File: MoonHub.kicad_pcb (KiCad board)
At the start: 4 copper layers, 250 x 16.5 mm, 33 parts, among them J1 USB_A, J2 USB_C_Receptacle_USB2.0, J3 USB_C_Receptacle_USB2.0, J4 USB_A, U1 SRV05-4, U2 SRV05-4, U3 CH334U, U4 TPS2552DBVR, Y1 12MHz

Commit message: second commmit
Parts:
- moved H4 83.8 mm to (164.2, 14.5)
- moved J2 65.1 mm to (157.1, 8.30)
- moved J4 47.9 mm to (190.9, 7.11)
- moved C8 4.90 mm to (204.3, 21.1)
- moved U1 1.50 mm to (27.8, 12.0)
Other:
- board size 250 x 16.5 mm -> 166.1 x 16.5 mm
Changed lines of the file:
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@@
   )
   (footprint "Capacitor_SMD:C_1206_3216Metric" (layer "F.Cu")
-    (at 200.775 24.5)
+    (at 204.3 21.1)
     (descr "Capacitor SMD 1206 (3216 Metric), square (rectangular) end terminal, IPC_7351 nominal, (Body size source: IPC-SM-782 page 76, https://www.pcb-3d.com/wordpress/wp-content/uploads/ipc-sm-782a_amendment_1_and_2.pdf), generated with kicad-footprint-generator")
     (tags "capacitor")
@@
         (effects (font (size 1 1) (thickness 0.15)))
     )
-    (pad "1" thru_hole circle (at 0 0) (size 3.500001 3.500001) (drill 2.2) (layers "*.Cu" "*.Mask")
+    (pad "1" thru_hole circle (at -83.7605 -0.1) (size 3.500001 3.500001) (drill 2.2) (layers "*.Cu" "*.Mask")
       (net 38 "GNDPWR") (pinfunction "1") (pintype "input"))
   )
@@
   )
   (footprint "MoonHub:Generic-Mounthole" (layer "F.Cu")
-    (at 248 14.5)
+    (at 164.2 14.5)
     (property "Sheetfile" "MoonHub.kicad_sch")
     (property "Sheetname" "")
@@
   )
   (footprint "MoonHub:TYPE-C-31-M-12" (layer "F.Cu")
-    (at 222.25 8.3 180)
+    (at 157.1375 8.3 180)
     (property "Sheetfile" "MoonHub.kicad_sch")
     (property "Sheetname" "")
@@
   )
   (footprint "MoonHub:USB-A-SMD_AF-APPLE-10.6" (layer "F.Cu")
-    (at 238.8 7.113 180)
+    (at 190.903 7.113 180)
     (property "Sheetfile" "MoonHub.kicad_sch")
     (property "Sheetname" "")
@@
   )
   (footprint "PCM_marbastlib-various:SOT-23-6-routable" (layer "F.Cu")
-    (at 27.75 10.5)
+    (at 27.75 12)
     (descr "SOT, 6 Pin (https://www.jedec.org/sites/default/files/docs/Mo-178c.PDF variant AB), generated with kicad-footprint-generator ipc_gullwing_generator.py")
     (tags "SOT TO_SOT_SMD")
@@
   (gr_line (start 0 14.5) (end 0 2)
     (stroke (width 0.1) (type default)) (layer "Edge.Cuts"))
-  (gr_line (start 250 14.5) (end 250 2)
+  (gr_line (start 166.1395 14.5) (end 166.1395 2)
     (stroke (width 0.1) (type default)) (layer "Edge.Cuts"))
-  (gr_arc (start 250 14.5) (mid 249.414214 15.914214) (end 248 16.5)
+  (gr_arc (start 166.1395 14.5) (mid 165.553714 15.914214) (end 164.1395 16.5)
     (stroke (width 0.1) (type default)) (layer "Edge.Cuts"))
   (gr_arc (start 2 16.5) (mid 0.585786 15.914214) (end 0 14.5)
@@
   (gr_arc (start 0 2) (mid 0.585786 0.585786) (end 2 0)
     (stroke (width 0.1) (type default)) (layer "Edge.Cuts"))
-  (gr_arc (start 248 0) (mid 249.414214 0.585786) (end 250 2)
+  (gr_arc (start 164.1395 0) (mid 165.553714 0.585786) (end 166.1395 2)
     (stroke (width 0.1) (type default)) (layer "Edge.Cuts"))
-  (gr_line (start 2 0) (end 248 0)
+  (gr_line (start 2 0) (end 164.1395 0)
     (stroke (width 0.1) (type default)) (layer "Edge.Cuts"))
-  (gr_line (start 248 16.5) (end 2 16.5)
+  (gr_line (start 164.1395 16.5) (end 2 16.5)
     (stroke (width 0.1) (type default)) (layer "Edge.Cuts"))
-  (segment (start 246.937 3.063) (end 247.9 2.1) (width 0.5) (layer "B.Cu") (net 38))
-  (segment (start 245.2 3.063) (end 246.937 3.063) (width 0.5) (layer "B.Cu") (net 38))
+  (segment (start 163.5395 2.6) (end 164.1395 2) (width 1) (layer "B.Cu") (net 38))
+  (segment (start 161.4375 2.6) (end 163.5395 2.6) (width 1) (layer "B.Cu") (net 38))
   (zone (net 6) (net_name "VBUS") (layer "F.Cu") (hatch edge 0.5)
     (priority 1)

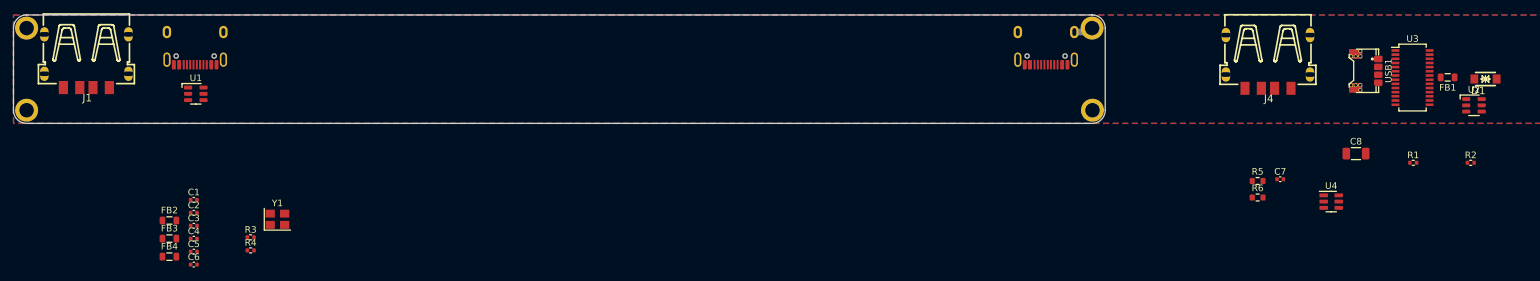
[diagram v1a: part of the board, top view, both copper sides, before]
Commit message: fully routed
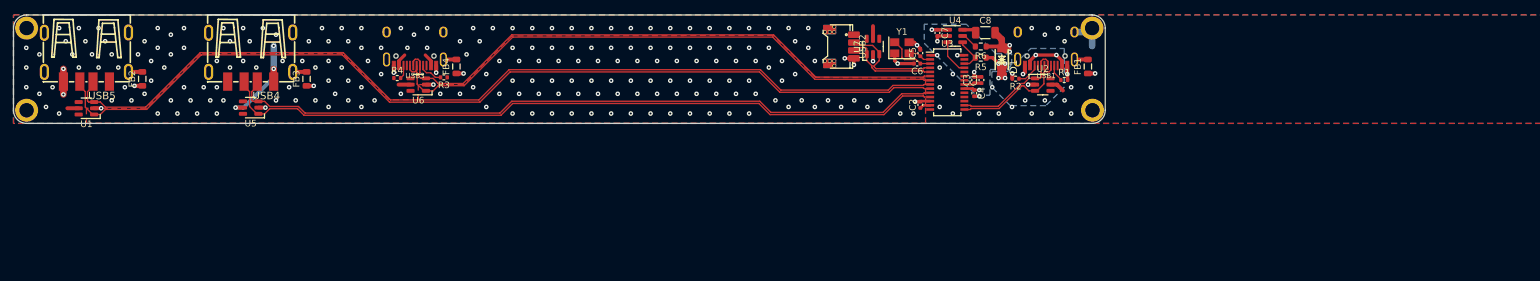
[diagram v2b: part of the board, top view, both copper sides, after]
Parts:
- added U5: SRV05-4, PCM_marbastlib-various:SOT-23-6-routable, F.Cu at (36.1, 14.1)
- added U6: SRV05-4, PCM_marbastlib-various:SOT-23-6-routable, F.Cu at (61.6, 10.6)
- added U7: SRV05-4, PCM_marbastlib-various:SOT-23-6-routable, F.Cu at (130.8, 4.80)
- USB1: renamed from J2; footprint MoonHub:TYPE-C-31-M-12 -> MoonHub:HRO-TYPE-C-31-M-12-Assembly
- USB2: renamed from USB1; footprint MoonHub:PicoEZMate-Reinforced-Alt -> MoonHub:PicoEZMate-Reinforced-Lite
- USB3: renamed from J3; footprint MoonHub:TYPE-C-31-M-12 -> MoonHub:HRO-TYPE-C-31-M-12-Assembly
- USB4: renamed from J4; footprint MoonHub:USB-A-SMD_AF-APPLE-10.6 -> MoonHub:USB-A-SMD_USB-M-21_914-441A2021S10200
- USB5: renamed from J1; footprint MoonHub:USB-A-SMD_AF-APPLE-10.6 -> MoonHub:USB-A-SMD_USB-M-21_914-441A2021S10200
- moved USB4 154.8 mm to (36.1, 6.40)
- moved C1 121.2 mm to (147.3, 9.90), turned to 90 degrees
- moved C3 120.8 mm to (146.2, 9.90), turned to 90 degrees
- moved C4 120.8 mm to (146.2, 11.9), turned to -90 degrees
- moved C5 114.6 mm to (138.0, 5.80), turned to 90 degrees
- moved C6 114.3 mm to (137.5, 7.40), turned to 180 degrees
- moved C2 111.8 mm to (138.0, 13.7), turned to 90 degrees
- moved Y1 98.5 mm to (135.2, 5.00)
- moved USB2 80.1 mm to (125.7, 4.80)
- moved D1 73.7 mm to (150.4, 6.80), turned to -90 degrees
- moved U3 70.8 mm to (142.1, 10.3)
- moved R2 70.4 mm to (152.5, 9.70), turned to 180 degrees
- moved U2 65.7 mm to (156.6, 10.6)
- moved U4 62.5 mm to (143.3, 3.20)
- moved C8 59.3 mm to (147.9, 2.70)
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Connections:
- C1 pad 1: +3V3 -> Net-(C1-Pad1)
- C2 pad 1: +3V3 -> Net-(C2-Pad1)
- C3 pad 1: +3V3 -> Net-(C1-Pad1)
- C5 pad 1: Net-(C5-Pad1) -> Net-(U3-XO)
- C6 pad 1: Net-(C6-Pad1) -> Net-(U3-XI)
- U1 pad 3: /USB2_D+ -> /USB1_D-
- U1 pad 4: /USB2_D- -> unconnected-(U1-IO3-Pad4)
- U1 pad 6: /USB1_D- -> unconnected-(U1-IO4-Pad6)
- U2 pad 3: /USB3_D+ -> /USBU_D-
- U2 pad 4: /USB3_D- -> unconnected-(U2-IO3-Pad4)
- U2 pad 6: /USBU_D- -> unconnected-(U2-IO4-Pad6)
- U3 pad 10: /USB1_D- -> /USB2_D-
- U3 pad 11: /USB1_D+ -> /USB2_D+
- U3 pad 13: +3V3 -> Net-(C2-Pad1)
- U3 pad 21: +3V3 -> Net-(C1-Pad1)
- U3 pad 8: /USB2_D- -> /USB1_D-
- U3 pad 9: /USB2_D+ -> /USB1_D+
- USB2 pad 1: +5V -> VBUS
- USB3 pad A6: /USB2_D+ -> /USB3_D+
- USB3 pad A7: /USB2_D- -> /USB3_D-
- USB3 pad B6: /USB2_D+ -> /USB3_D+
- USB3 pad B7: /USB2_D- -> /USB3_D-
- USB4 pad 2: /USB3_D- -> /USB2_D-
- USB4 pad 3: /USB3_D+ -> /USB2_D+
- Y1 pad 1: Net-(C5-Pad1) -> GND
- Y1 pad 3: Net-(C6-Pad1) -> GND
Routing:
- net /USB1_D+: track 0.00 -> 143.6 mm
- net /USB1_D-: track 0.00 -> 141.9 mm
- net /USB2_D+: track 0.00 -> 111.6 mm
- net /USB2_D-: track 0.00 -> 109.9 mm
- net /USB3_D+: track 0.00 -> 90.0 mm
- net /USB3_D-: track 0.00 -> 88.3 mm
- net GND: track 0.00 -> 47.8 mm, vias 0 -> 251
- net VBUS: track 0.00 -> 29.4 mm, vias 0 -> 3
- net +5V: track 0.00 -> 21.1 mm, vias 0 -> 8
- net /USBU_D-: track 0.00 -> 19.8 mm
- net /USBU_D+: track 0.00 -> 18.0 mm
- net /USB4_D-: track 0.00 -> 15.7 mm
- net /USB4_D+: track 0.00 -> 14.5 mm
- net GNDPWR: track 2.95 -> 13.9 mm
- net Net-(U3-XI): track 0.00 -> 7.48 mm
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- added copper zone on B.Cu, net +5V
- added copper zone on F.Cu, net GND
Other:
- rule pad_to_mask_clearance: 0 -> 0.038

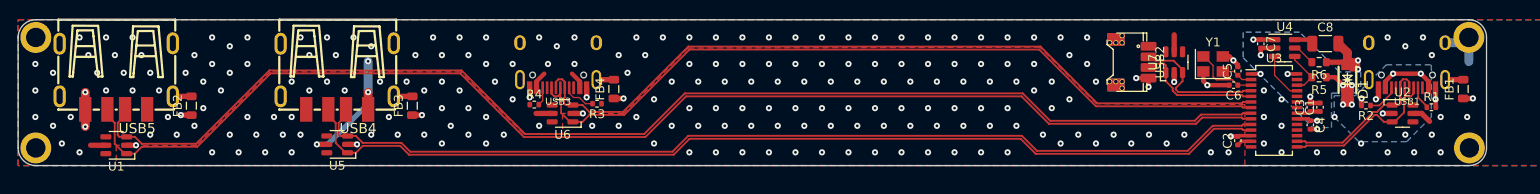
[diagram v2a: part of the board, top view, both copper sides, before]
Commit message: reroute for smaller size
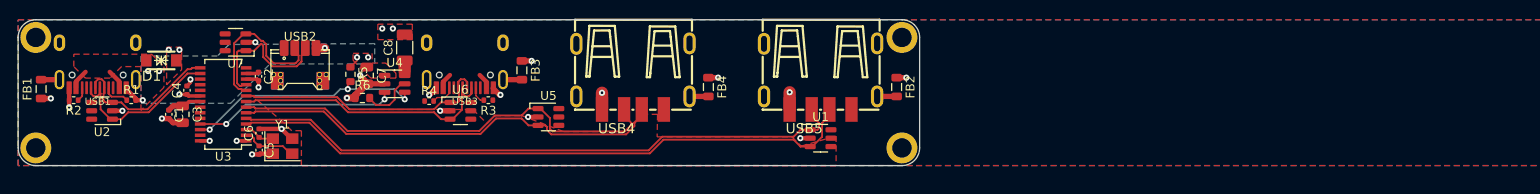
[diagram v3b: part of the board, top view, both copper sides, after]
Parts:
- C3, C7: footprint Capacitor_SMD:C_0402_1005Metric -> Capacitor_SMD:C_0805_2012Metric
- moved H2 245.9 mm to (2.00, 2.00)
- moved FB1 160.9 mm to (2.60, 7.84)
- moved USB1 148.1 mm to (9.00, 0.00)
- moved U2 147.1 mm to (9.50, 10.3), turned to 180 degrees
- moved R1 147.1 mm to (12.8, 9.10)
- moved R2 146.2 mm to (6.28, 9.10)
- moved D1 134.2 mm to (16.2, 4.60), turned to 180 degrees
- moved C1 130.3 mm to (17.1, 10.7), turned to -90 degrees
- moved C3 127.6 mm to (18.6, 10.7), turned to -90 degrees
- moved C4 127.2 mm to (19.1, 7.97), turned to 90 degrees
- moved U3 118.9 mm to (23.2, 9.57), turned to 180 degrees
- moved C5 111.1 mm to (27.3, 14.8), turned to -90 degrees
- moved C2 111.0 mm to (27.2, 6.40), turned to -90 degrees
- moved C6 110.4 mm to (27.3, 12.8), turned to 90 degrees
- moved R5 109.6 mm to (37.6, 6.17), turned to -90 degrees
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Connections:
- U1 pad 1: /USB1_D+ -> /USB4_D+
- U1 pad 3: /USB1_D- -> /USB4_D-
- U3 pad 10: /USB2_D- -> /USB1_D-
- U3 pad 11: /USB2_D+ -> /USB1_D+
- U3 pad 8: /USB1_D- -> /USB2_D-
- U3 pad 9: /USB1_D+ -> /USB2_D+
- U5 pad 1: /USB2_D+ -> /USB3_D+
- U5 pad 3: /USB2_D- -> /USB3_D-
- U6 pad 1: /USB3_D+ -> /USB2_D+
- U6 pad 3: /USB3_D- -> /USB2_D-
- U7 pad 1: /USB4_D+ -> /USB1_D+
- U7 pad 3: /USB4_D- -> /USB1_D-
- USB2 pad 2: /USB4_D- -> /USB1_D-
- USB2 pad 3: /USB4_D+ -> /USB1_D+
- USB3 pad A6: /USB3_D+ -> /USB2_D+
- USB3 pad A7: /USB3_D- -> /USB2_D-
- USB3 pad B6: /USB3_D+ -> /USB2_D+
- USB3 pad B7: /USB3_D- -> /USB2_D-
- USB4 pad 2: /USB2_D- -> /USB3_D-
- USB4 pad 3: /USB2_D+ -> /USB3_D+
- USB5 pad 2: /USB1_D- -> /USB4_D-
- USB5 pad 3: /USB1_D+ -> /USB4_D+
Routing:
- net /USB1_D+: track 143.6 -> 16.2 mm
- net /USB1_D-: track 141.9 -> 17.9 mm
- net /USB2_D+: track 111.6 -> 29.2 mm
- net /USB2_D-: track 109.9 -> 30.9 mm
- net /USB4_D-: track 15.7 -> 71.5 mm
- net /USB4_D+: track 14.5 -> 69.8 mm
- net /USB3_D+: track 90.0 -> 49.9 mm
- net /USB3_D-: track 88.3 -> 49.3 mm
- net VBUS: track 29.4 -> 4.42 mm, vias 3 -> 0
- net /OVCUR: track 5.20 -> 27.3 mm, vias 0 -> 3
- net /PWREN: track 5.40 -> 22.8 mm, vias 0 -> 2
- net +5V: track 21.1 -> 8.32 mm, vias 8 -> 5
- net GNDPWR: track 13.9 -> 8.56 mm
- net GND: track 47.8 -> 42.7 mm, vias 251 -> 29
- net Net-(U3-XI): track 7.48 -> 3.46 mm
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- added copper zone on F.Cu, net +5V
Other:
- board size 166.1 x 16.5 mm -> 102 x 16.5 mm

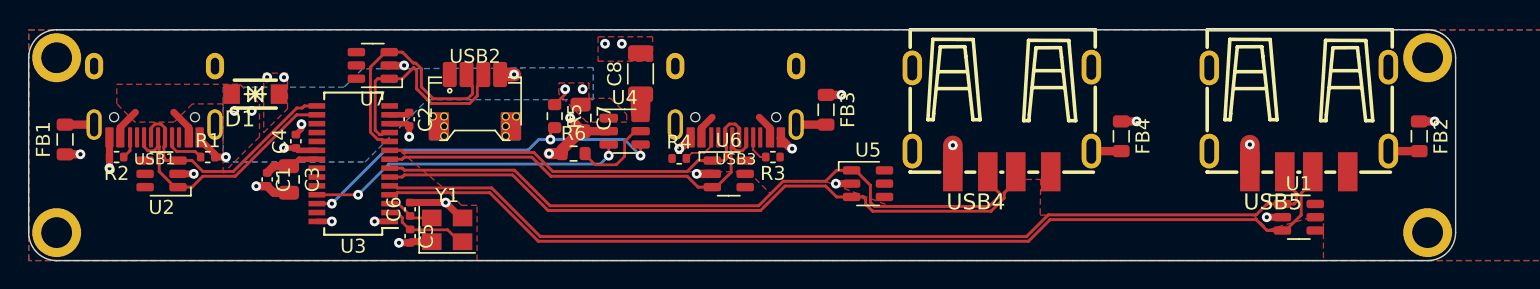
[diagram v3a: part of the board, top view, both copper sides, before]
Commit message: move uDB connector & switch current limit
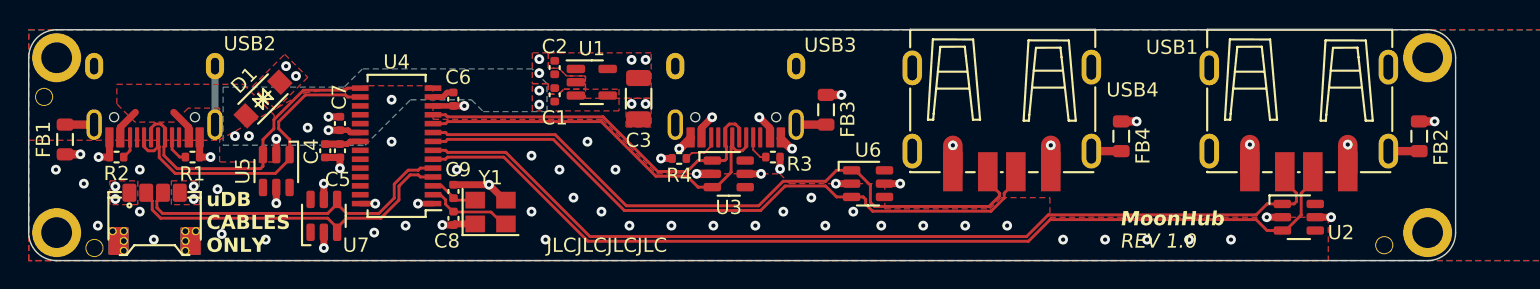
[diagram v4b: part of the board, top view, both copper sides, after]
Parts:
- removed the C7 at (39.5, 6.30)
- removed the C8 at (43.7, 3.15)
- removed R5: 100k, Resistor_SMD:R_0603_1608Metric
- removed R6: 27k, Resistor_SMD:R_0603_1608Metric
- removed the U4 at (42.6, 7.25)
- removed the USB2 at (31.9, 5.40)
- added C1: 1u, Capacitor_SMD:C_0402_1005Metric, F.Cu at (37.6, 4.65)
- added C2: 100n, Capacitor_SMD:C_0402_1005Metric, F.Cu at (37.6, 2.70)
- added C3: 100u, Capacitor_SMD:C_1206_3216Metric, F.Cu at (43.6, 4.92)
- added G***: LOGO, LOGO, B.Cu at (70.2, 2.20)
- added G***: LOGO, LOGO, B.Cu at (51.2, 2.10)
- added G***: LOGO, LOGO, B.Cu at (9.00, 2.10)
- added G***: LOGO, LOGO, B.Cu at (91.4, 2.10)
- added H5: ToolingHole, MoonHub:JLC-Tooling-Hole, F.Cu at (1.10, 4.80)
- added H6: ToolingHole, MoonHub:JLC-Tooling-Hole, F.Cu at (4.70, 15.6)
- added H7: ToolingHole, MoonHub:JLC-Tooling-Hole, F.Cu at (96.9, 15.4)
- added J1: X1224WRS-04-LPV01, MoonHub:UDB-PicoEZMate-Reinforced-Alt, F.Cu at (9.00, 13.6)
- added U1: AP22818AKBWT-7, Package_TO_SOT_SMD:SOT-23-5, F.Cu at (40.2, 3.75)
- C5: renamed from C3; footprint Capacitor_SMD:C_0805_2012Metric -> Capacitor_SMD:C_0402_1005Metric
- moved U7 11.3 mm to (21.1, 13.3), turned to 90 degrees
- moved U5 8.20 mm to (17.7, 10.1), turned to -90 degrees
- moved C4 4.63 mm to (21.2, 8.65)
- moved C5 4.19 mm to (22.2, 8.65)
- moved C6 3.46 mm to (30.4, 4.96)
- moved C7 3.40 mm to (22.2, 6.70)
- moved Y1 3.35 mm to (33.0, 13.0)
- moved U4 3.35 mm to (26.3, 8.30)
- moved C8 3.35 mm to (30.4, 13.5)
- moved C9 3.35 mm to (30.4, 11.6)
- moved R1 1.09 mm to (11.7, 9.10)
- moved D1 0.65 mm to (16.8, 4.95), turned to -135 degrees
- renumbered C1 to C4, C2 to C6, C4 to C7, C5 to C8, C6 to C9, U1 to U2, U6 to U3, U3 to U4, U2 to U5, U5 to U6, USB5 to USB1, USB1 to USB2
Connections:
- U2 pad 1: /USB4_D+ -> /USB3_D+
- U2 pad 3: /USB4_D- -> /USB3_D-
- U3 pad 1: /USB2_D+ -> /USB1_D+
- U3 pad 3: /USB2_D- -> /USB1_D-
- U6 pad 1: /USB3_D+ -> /USB2_D+
- U6 pad 3: /USB3_D- -> /USB2_D-
- U7 pad 1: /USB1_D+ -> unconnected-(U7-IO1-Pad1)
- U7 pad 3: /USB1_D- -> /USB4_D-
- U7 pad 4: unconnected-(U7-IO3-Pad4) -> /USB4_D+
- USB1 pad 2: /USB4_D- -> /USB3_D-
- USB1 pad 3: /USB4_D+ -> /USB3_D+
- USB3 pad A6: /USB2_D+ -> /USB1_D+
- USB3 pad A7: /USB2_D- -> /USB1_D-
- USB3 pad B6: /USB2_D+ -> /USB1_D+
- USB3 pad B7: /USB2_D- -> /USB1_D-
- USB4 pad 2: /USB3_D- -> /USB2_D-
- USB4 pad 3: /USB3_D+ -> /USB2_D+
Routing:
- net /USB4_D-: track 71.5 -> 24.5 mm
- net /USB4_D+: track 69.8 -> 24.0 mm
- net /OVCUR: track 27.3 -> 0.00 mm, vias 3 -> 0
- net /PWREN: track 22.8 -> 0.00 mm, vias 2 -> 0
- net /USB3_D-: track 49.3 -> 69.5 mm
- net /USB2_D+: track 29.2 -> 47.9 mm
- net /USB3_D+: track 49.9 -> 67.8 mm
- net /USB2_D-: track 30.9 -> 47.3 mm
- net /USB1_D+: track 16.2 -> 27.2 mm
- net /USB1_D-: track 17.9 -> 28.9 mm
- net VBUS: track 4.42 -> 14.6 mm, vias 0 -> 15
- net GND: track 42.7 -> 34.2 mm, vias 29 -> 70
- net Net-(U4-ILIM): track 5.95 -> 0.00 mm
- net /USBU_D+: track 18.9 -> 23.9 mm
- net /USBU_D-: track 17.4 -> 22.2 mm
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- added copper zone on F.Cu, net GNDPWR
- added copper zone on B.Cu, net VBUS
- removed copper zone on B.Cu, net GNDPWR
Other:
- board text added: "0.5A"
- board text added: "1"
- board text added: "2"
- board text added: "3"
- board text added: "5V"
- board text added: "JLCJLCJLCJLC"
- board text added: "MoonHub"
- board text added: "REV 1.0"
- board text added: "UPSTREAM"
- board text added: "uDB CABLES ONLY"

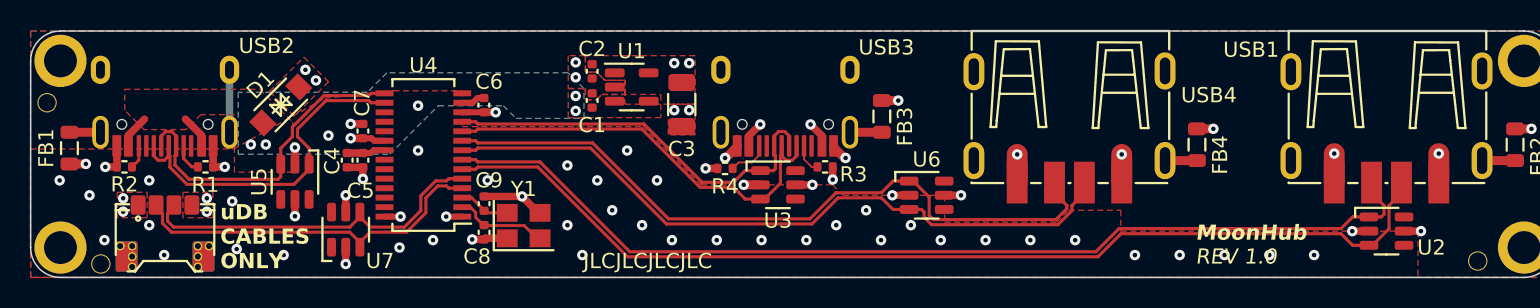
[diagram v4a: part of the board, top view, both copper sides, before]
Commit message: redo esd protection
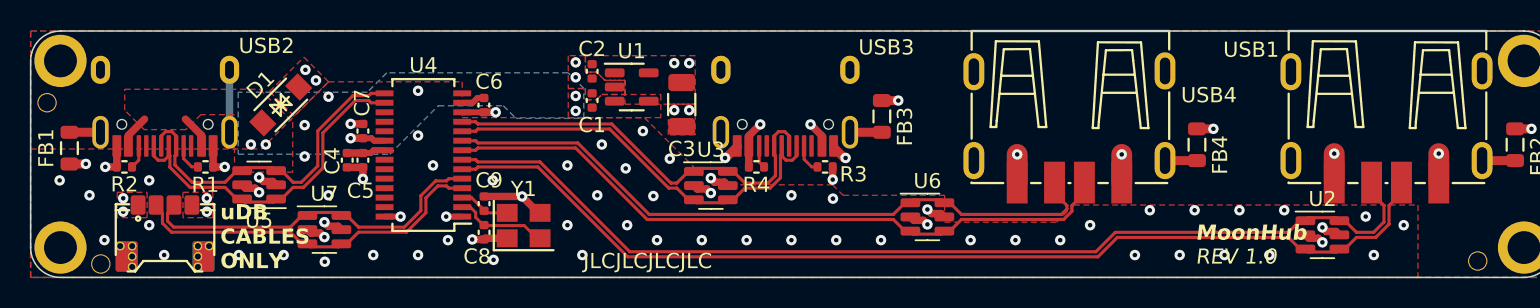
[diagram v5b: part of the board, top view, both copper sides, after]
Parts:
- U2, U3, U5, U6, U7: footprint PCM_marbastlib-various:SOT-23-6-routable -> Package_TO_SOT_SMD:SOT-23-6
- moved U3 4.49 mm to (45.5, 10.3)
- moved U2 4.30 mm to (86.5, 13.7)
- moved U5 2.41 mm to (15.3, 10.3), turned to 180 degrees
- moved R4 2.10 mm to (48.6, 9.10)
- moved U6 1.45 mm to (60.0, 12.4)
- moved U7 1.43 mm to (19.7, 13.3), turned to 0 degrees
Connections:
- U2 pad 4: unconnected-(U2-IO3-Pad4) -> /USB3_D-
- U2 pad 6: unconnected-(U2-IO4-Pad6) -> /USB3_D+
- U3 pad 4: unconnected-(U3-IO3-Pad4) -> /USB1_D-
- U3 pad 6: unconnected-(U3-IO4-Pad6) -> /USB1_D+
- U5 pad 4: unconnected-(U5-IO3-Pad4) -> /USBU_D-
- U5 pad 6: unconnected-(U5-IO4-Pad6) -> /USBU_D+
- U6 pad 4: unconnected-(U6-IO3-Pad4) -> /USB2_D-
- U6 pad 6: unconnected-(U6-IO4-Pad6) -> /USB2_D+
- U7 pad 1: unconnected-(U7-IO1-Pad1) -> /USB4_D+
- U7 pad 4: /USB4_D+ -> /USB4_D-
- U7 pad 6: unconnected-(U7-IO4-Pad6) -> /USB4_D+
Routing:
- net /USB2_D+: track 47.9 -> 45.6 mm
- net VBUS: track 14.6 -> 16.3 mm, vias 15 -> 14
- net Net-(USB3-CC2): track 2.76 -> 1.54 mm
- net /USB1_D+: track 27.2 -> 28.3 mm
- net /USB3_D+: track 67.8 -> 68.9 mm
- net /USB2_D-: track 47.3 -> 46.2 mm
- net GND: track 34.2 -> 35.3 mm, vias 70 -> 84
- net /USBU_D-: track 22.2 -> 23.1 mm

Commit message: export step
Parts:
- added G***: LOGO, LOGO, B.Cu at (11.6, 12.2)
- added REF**: OSHW-Logo2_9.8x8mm_SilkScreen, Symbol:OSHW-Logo2_9.8x8mm_SilkScreen, B.Cu at (91.5, 12.2)
- moved FB2 17.6 mm to (82.1, 4.28), turned to 90 degrees
- moved FB4 3.35 mm to (78.2, 4.26), turned to 90 degrees
- moved USB1 0.40 mm to (90.8, 6.81)
- moved USB4 0.40 mm to (69.6, 6.81)
- moved U2 0.25 mm to (86.5, 13.9)
- moved U6 0.20 mm to (60.0, 12.7)
